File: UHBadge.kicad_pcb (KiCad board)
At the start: 2 copper layers, 0 parts

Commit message: Added footprints.
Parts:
- added C1: 4.7uF, Capacitor_SMD:C_0402_1005Metric, F.Cu at (153.6, 54.0)
- added C10: 100nF, Capacitor_SMD:C_0402_1005Metric, F.Cu at (156.5, 57.9)
- added C11: 100nF, Capacitor_SMD:C_0402_1005Metric, F.Cu at (156.5, 59.9)
- added C12: 100nF, Capacitor_SMD:C_0402_1005Metric, F.Cu at (156.5, 61.9)
- added C13: 100nF, Capacitor_SMD:C_0402_1005Metric, F.Cu at (156.5, 63.8)
- added C14: 100nF, Capacitor_SMD:C_0402_1005Metric, F.Cu at (156.5, 65.8)
- added C15: 100nF, Capacitor_SMD:C_0402_1005Metric, F.Cu at (159.3, 54.0)
- added C16: 4.7uF, Capacitor_SMD:C_0402_1005Metric, F.Cu at (159.3, 56.0)
- added C17: 4.7uF, Capacitor_SMD:C_0402_1005Metric, F.Cu at (159.3, 57.9)
- added C18: 10uF, Capacitor_SMD:C_0402_1005Metric, F.Cu at (159.3, 59.9)
- added C19: 100nF, Capacitor_SMD:C_0402_1005Metric, F.Cu at (159.3, 61.9)
- added C2: 4.7uF, Capacitor_SMD:C_0402_1005Metric, F.Cu at (153.6, 56.0)
- added C20: 15pF, Capacitor_SMD:C_0402_1005Metric, F.Cu at (159.3, 63.8)
- added C21: 15pF, Capacitor_SMD:C_0402_1005Metric, F.Cu at (159.3, 65.8)
- added C22: 33pF, Capacitor_SMD:C_0402_1005Metric, F.Cu at (162.2, 54.0)
- added C23: 0.1uF, Capacitor_SMD:C_0402_1005Metric, F.Cu at (162.2, 56.0)
- added C24: 1uF, Capacitor_SMD:C_0402_1005Metric, F.Cu at (162.2, 57.9)
- added C25: 1uF, Capacitor_SMD:C_0402_1005Metric, F.Cu at (162.2, 59.9)
- added C26: 1uF, Capacitor_SMD:C_0402_1005Metric, F.Cu at (162.2, 61.9)
- added C27: 1uF, Capacitor_SMD:C_0402_1005Metric, F.Cu at (162.2, 63.8)
- added C28: 1uF, Capacitor_SMD:C_0402_1005Metric, F.Cu at (162.2, 65.8)
- added C29: 1uF, Capacitor_SMD:C_0402_1005Metric, F.Cu at (165.1, 54.0)
- added C3: 4.7uF, Capacitor_SMD:C_0402_1005Metric, F.Cu at (153.6, 57.9)
- added C30: 1uF, Capacitor_SMD:C_0402_1005Metric, F.Cu at (165.1, 56.0)
- added C31: 1uF, Capacitor_SMD:C_0402_1005Metric, F.Cu at (165.1, 57.9)
- added C32: 1uF, Capacitor_SMD:C_0402_1005Metric, F.Cu at (165.1, 59.9)
- added C33: 1uF, Capacitor_SMD:C_0402_1005Metric, F.Cu at (165.1, 61.9)
- added C34: 4.7uF, Capacitor_SMD:C_0402_1005Metric, F.Cu at (165.1, 63.8)
- added C35: 4.7uF, Capacitor_SMD:C_0402_1005Metric, F.Cu at (165.1, 65.8)
- added C4: 100nF, Capacitor_SMD:C_0402_1005Metric, F.Cu at (153.6, 59.9)
- added C5: 4.7uF, Capacitor_SMD:C_0402_1005Metric, F.Cu at (153.6, 61.9)
- added C6: 100nF, Capacitor_SMD:C_0402_1005Metric, F.Cu at (153.6, 63.8)
- added C7: 100nF, Capacitor_SMD:C_0402_1005Metric, F.Cu at (153.6, 65.8)
- added C8: 100nF, Capacitor_SMD:C_0402_1005Metric, F.Cu at (156.5, 54.0)
- added C9: 100nF, Capacitor_SMD:C_0402_1005Metric, F.Cu at (156.5, 56.0)
- added D1: LED, LED_SMD:LED_0805_2012Metric, F.Cu at (160.3, 68.3)
- added D2: LED, LED_SMD:LED_0805_2012Metric, F.Cu at (160.3, 71.3)
- added D3: LED, LED_SMD:LED_0805_2012Metric, F.Cu at (160.3, 74.4)
- added D4: LED, LED_SMD:LED_0805_2012Metric, F.Cu at (160.3, 77.4)
- added D5: MBR0530, Diode_SMD:D_SOD-123, F.Cu at (120.9, 93.6)
- added D6: MBR0530, Diode_SMD:D_SOD-123, F.Cu at (120.9, 97.0)
- added D7: MBR0530, Diode_SMD:D_SOD-123, F.Cu at (120.9, 100.3)
- added H1: MountingHole_Pad, MountingHole:MountingHole_2.2mm_M2_Pad_Via, F.Cu at (155.1, 69.8)
- added H2: MountingHole_Pad, MountingHole:MountingHole_2.2mm_M2_Pad_Via, F.Cu at (155.1, 75.7)
- added J1: Conn_01x03_MountingPin, Connector_PinHeader_1.00mm:PinHeader_1x03_P1.00mm_Vertical, F.Cu at (141.9, 99.6)
- added J2: Conn_01x10_MountingPin, Connector_PinHeader_1.00mm:PinHeader_1x10_P1.00mm_Vertical, F.Cu at (164.2, 68.3)
- added L1: 3.3u, CustomFootprints:Inductor, F.Cu at (163.2, 102.9)
- added L2: NFC Antenna, CustomFootprints:NFC_Antenna, F.Cu at (127.2, 91.2)
- added L3: 47uH 500mA, Inductor_SMD:L_APV_ANR4018, F.Cu at (158.3, 100.1)
- added P1: USB_C_Plug_USB2.0, Connector_USB:USB_C_Receptacle_GCT_USB4105-xx-A_16P_TopMnt_Horizontal, F.Cu at (140.9, 93.3)
- added Q1: Si1308EDL, Package_TO_SOT_SMD:SOT-323_SC-70, F.Cu at (132.4, 93.7)
- added R1: 33Ω, Resistor_SMD:R_0402_1005Metric, F.Cu at (148.2, 89.0)
- added R10: 1kΩ, Resistor_SMD:R_0402_1005Metric, F.Cu at (151.2, 95.0)
- added R11: 1kΩ, Resistor_SMD:R_0402_1005Metric, F.Cu at (151.2, 97.0)
- added R12: 10kΩ, Resistor_SMD:R_0402_1005Metric, F.Cu at (151.2, 99.0)
- added R13: 10kΩ, Resistor_SMD:R_0402_1005Metric, F.Cu at (154.1, 89.0)
- added R14: 10kΩ, Resistor_SMD:R_0402_1005Metric, F.Cu at (154.1, 91.0)
- added R15: 47Ω, Resistor_SMD:R_0402_1005Metric, F.Cu at (154.1, 93.0)
- added R16: 1MΩ, Resistor_SMD:R_0402_1005Metric, F.Cu at (154.1, 95.0)
- added R17: 2.2Ω, Resistor_SMD:R_0402_1005Metric, F.Cu at (154.1, 97.0)
- added R2: 27Ω, Resistor_SMD:R_0402_1005Metric, F.Cu at (148.2, 91.0)
- added R3: 27Ω, Resistor_SMD:R_0402_1005Metric, F.Cu at (148.2, 93.0)
- added R4: 5.1kΩ, Resistor_SMD:R_0402_1005Metric, F.Cu at (148.2, 95.0)
- added R5: 470Ω, Resistor_SMD:R_0402_1005Metric, F.Cu at (148.2, 97.0)
- added R6: 470Ω, Resistor_SMD:R_0402_1005Metric, F.Cu at (148.2, 99.0)
- added R7: 470Ω, Resistor_SMD:R_0402_1005Metric, F.Cu at (151.2, 89.0)
- added R8: 0Ω, Resistor_SMD:R_0402_1005Metric, F.Cu at (151.2, 91.0)
- added R9: 1kΩ, Resistor_SMD:R_0402_1005Metric, F.Cu at (151.2, 93.0)
- added SW1: Boot, Button_Switch_THT:SW_PUSH-12mm_Wuerth-430476085716, F.Cu at (137.4, 57.3)
- added SW2: Run, Button_Switch_THT:SW_PUSH-12mm_Wuerth-430476085716, F.Cu at (137.4, 70.8)
- added U1: RP2350A, Package_DFN_QFN:QFN-60-1EP_7x7mm_P0.4mm_EP3.4x3.4mm, F.Cu at (160.5, 92.7)
- added U2: MCP73871, Package_DFN_QFN:QFN-20-1EP_4x4mm_P0.5mm_EP2.5x2.5mm, F.Cu at (127.3, 95.1)
- added U3: W25Q128JVS, Package_SO:SOIC-8_5.3x5.3mm_P1.27mm, F.Cu at (159.9, 83.6)
- added U4: SRV05-4, Package_TO_SOT_SMD:SOT-23-6, F.Cu at (137.7, 100.4)
- added U5: Conn, Connector_FFC-FPC:Jushuo_AFC07-S24FCA-00_1x24-1MP_P0.50_Horizontal, F.Cu at (144.9, 83.4)
- added U6: ST25DV64K-JFR6D3, Package_DFN_QFN:ST_UFDFPN-12-1EP_3x3mm_P0.5mm_EP1.4x2.55mm, F.Cu at (126.8, 100.5)
- added Y1: ABM8-272-T3, Crystal:Crystal_SMD_3225-4Pin_3.2x2.5mm, F.Cu at (132.1, 100.5)

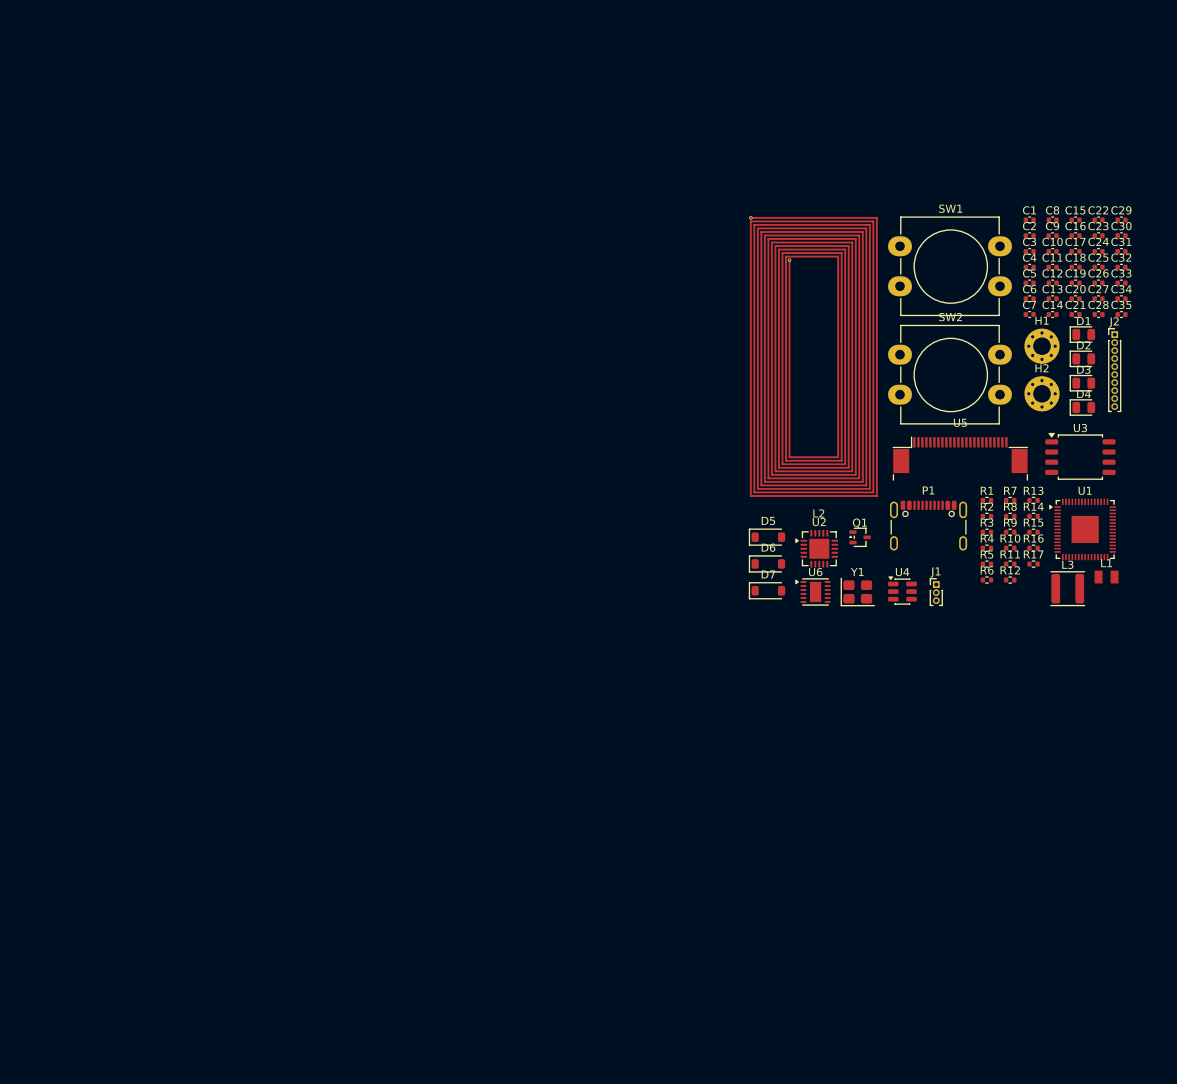
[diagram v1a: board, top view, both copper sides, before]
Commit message: Created the Badge borders. Fixed the buttons footprints.
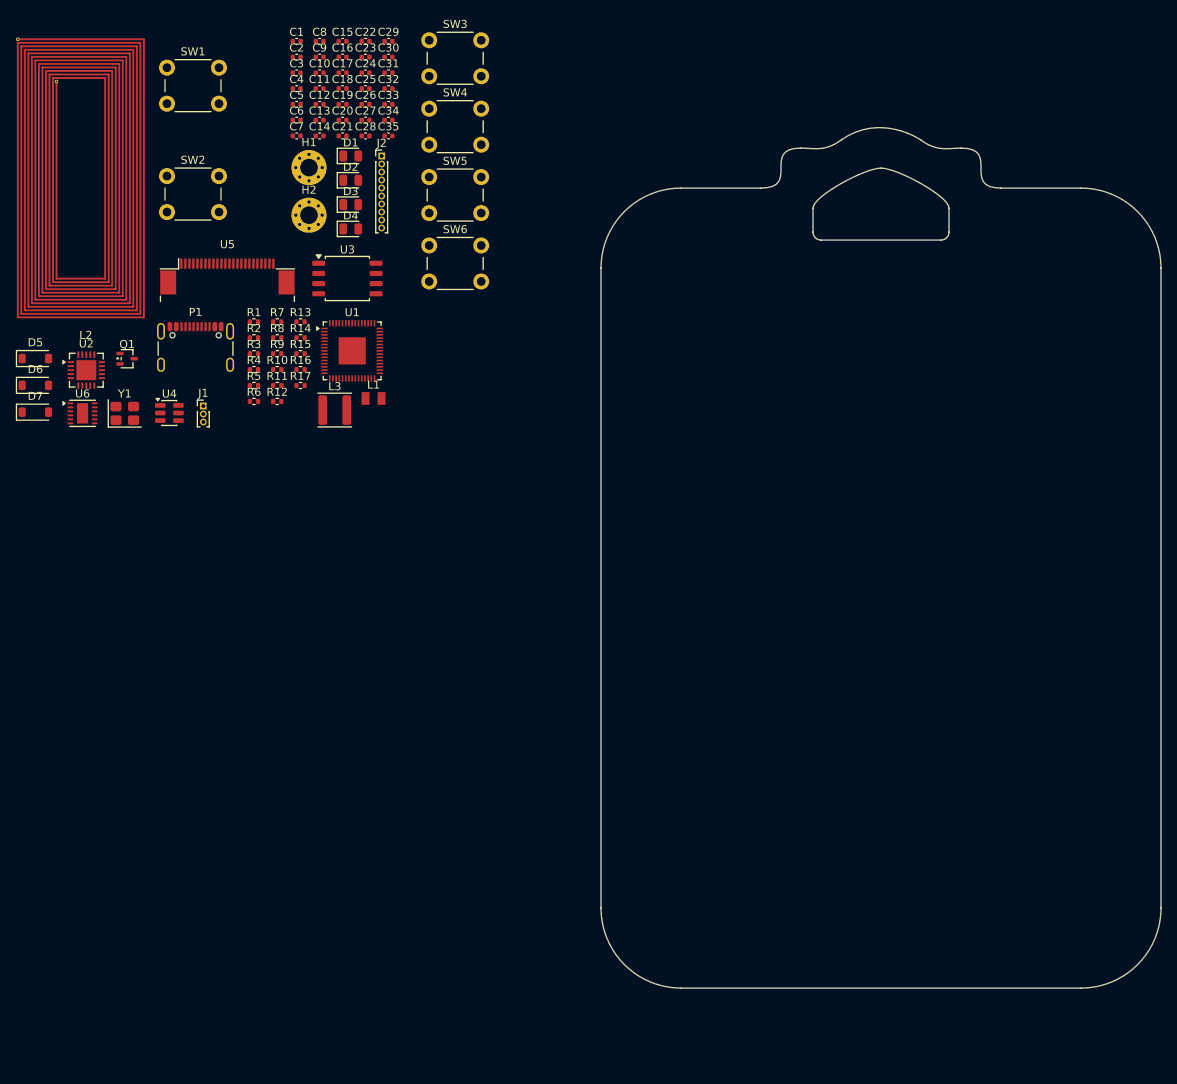
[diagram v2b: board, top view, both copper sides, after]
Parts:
- added SW3: Up, Button_Switch_THT:SW_PUSH_6mm, F.Cu at (78.5, 31.5)
- added SW4: Down, Button_Switch_THT:SW_PUSH_6mm, F.Cu at (78.5, 40.1)
- added SW5: Left, Button_Switch_THT:SW_PUSH_6mm, F.Cu at (78.5, 48.6)
- added SW6: Right, Button_Switch_THT:SW_PUSH_6mm, F.Cu at (78.5, 57.2)
- SW1, SW2: footprint Button_Switch_THT:SW_PUSH-12mm_Wuerth-430476085716 -> Button_Switch_THT:SW_PUSH_6mm
- moved C10 94.3 mm to (64.8, 35.6)
- moved C11 94.3 mm to (64.8, 37.6)
- moved C12 94.3 mm to (64.8, 39.5)
- moved C13 94.3 mm to (64.8, 41.5)
- moved C14 94.3 mm to (64.8, 43.5)
- moved C8 94.3 mm to (64.8, 31.7)
- moved C9 94.3 mm to (64.8, 33.6)
- moved U1 94.3 mm to (68.9, 70.3)
- moved U3 94.3 mm to (68.3, 61.3)
- moved U4 94.3 mm to (46.0, 78.1)
- moved U5 94.3 mm to (53.3, 61.0)
- moved C1 94.3 mm to (62.0, 31.7)
- moved C2 94.3 mm to (62.0, 33.6)
- moved C22 94.3 mm to (70.6, 31.7)
- moved C23 94.3 mm to (70.6, 33.6)
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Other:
- board outline added: 70 x 107.6 mm

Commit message: Connected the buttons to the RP2350.
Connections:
- U1 pad 10: unconnected-(U1-GPIO7-Pad10) -> DOWN
- U1 pad 12: unconnected-(U1-GPIO8-Pad12) -> LEFT
- U1 pad 13: unconnected-(U1-GPIO9-Pad13) -> RIGHT
- U1 pad 9: unconnected-(U1-GPIO6-Pad9) -> UP
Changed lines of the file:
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@@
 			(layers "F.Cu" "F.Mask" "F.Paste")
 			(roundrect_rratio 0.25)
-			(net "unconnected-(U1-GPIO6-Pad9)")
+			(net "UP")
 			(pinfunction "GPIO6_9")
 			(pintype "bidirectional")
@@
 			(layers "F.Cu" "F.Mask" "F.Paste")
 			(roundrect_rratio 0.25)
-			(net "unconnected-(U1-GPIO7-Pad10)")
+			(net "DOWN")
 			(pinfunction "GPIO7_10")
 			(pintype "bidirectional")
@@
 			(layers "F.Cu" "F.Mask" "F.Paste")
 			(roundrect_rratio 0.25)
-			(net "unconnected-(U1-GPIO8-Pad12)")
+			(net "LEFT")
 			(pinfunction "GPIO8_12")
 			(pintype "bidirectional")
@@
 			(layers "F.Cu" "F.Mask" "F.Paste")
 			(roundrect_rratio 0.25)
-			(net "unconnected-(U1-GPIO9-Pad13)")
+			(net "RIGHT")
 			(pinfunction "GPIO9_13")
 			(pintype "bidirectional")

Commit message: Added the e-ink display. Made the button design.
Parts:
- L2, U5: moved to B.Cu
- SW1, SW2, SW3, SW4, SW5, SW6: footprint Button_Switch_THT:SW_PUSH_6mm -> Button_Switch_SMD:SW_SPST_EVQP2_MiddlePushTravel_H2.5mm
- moved L2 126.7 mm to (152.7, 117.3)
- moved SW5 108.8 mm to (120.1, 149.2)
- moved SW4 107.8 mm to (112.5, 142.4), turned to 90 degrees
- moved SW6 106.7 mm to (132.6, 149.2)
- moved SW3 104.2 mm to (112.5, 130.0), turned to 90 degrees
- moved U5 82.0 mm to (135.0, 68.0)
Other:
- board size 70 x 107.6 mm -> 70 x 117.6 mm

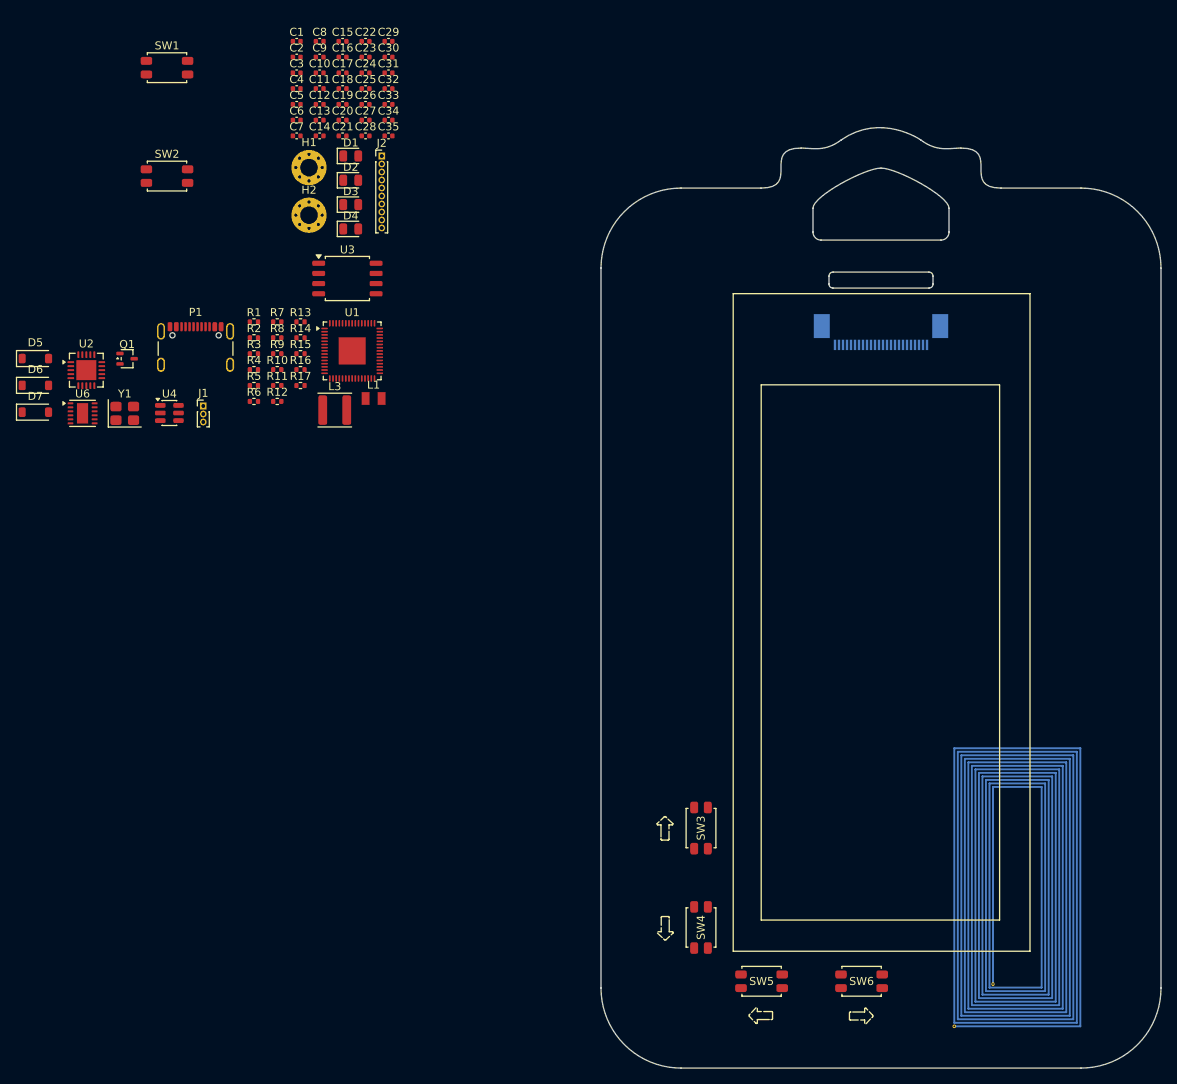
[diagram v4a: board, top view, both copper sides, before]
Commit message: Connected the support components to the e-ink display. Placed the RP2350 and started connecting the support components.
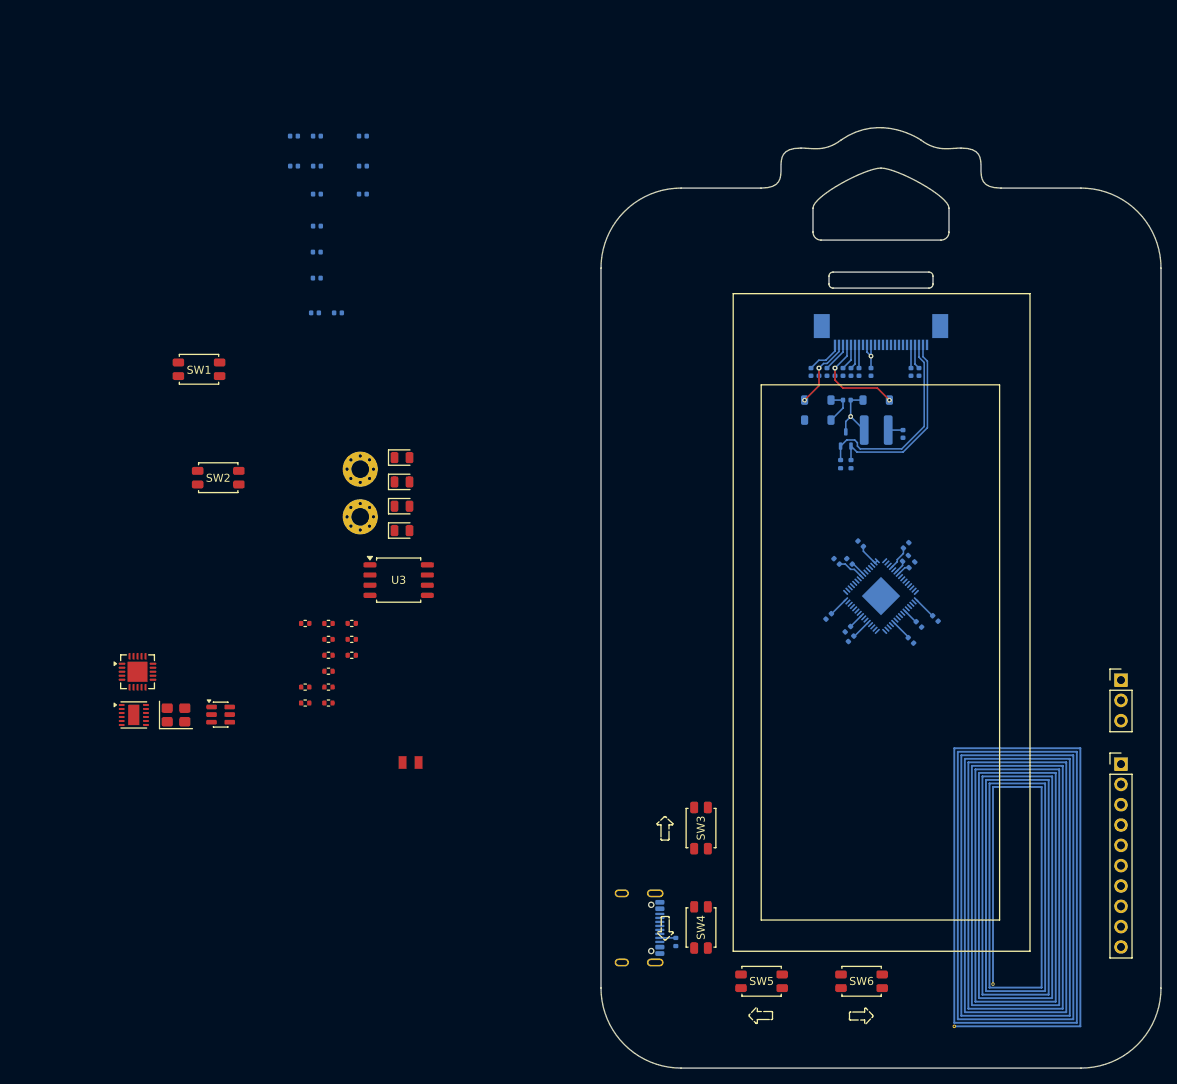
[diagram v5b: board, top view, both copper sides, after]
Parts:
- C1, C10, C11, C12, C13, C14, C15, C16, C17, C18, C19, C2, C20, C21, C22, C23, C24, C25, C26, C27, C28, C29, C3, C30, C31, C32, C33, C34, C35, C4, C6, C7, C8, C9, D5, D6, D7, L3, P1, Q1, R16, R17, R2, R3, R4, U1: moved to B.Cu
- C5: value 4.7uF -> 100nF; moved to B.Cu
- J1: footprint Connector_PinHeader_1.00mm:PinHeader_1x03_P1.00mm_Vertical -> Connector_PinHeader_2.54mm:PinHeader_1x03_P2.54mm_Vertical
- J2: footprint Connector_PinHeader_1.00mm:PinHeader_1x10_P1.00mm_Vertical -> Connector_PinHeader_2.54mm:PinHeader_1x10_P2.54mm_Vertical
- moved J1 119.7 mm to (165.0, 111.5)
- moved J2 119.7 mm to (165.0, 122.0)
- moved D7 105.1 mm to (134.4, 76.5), turned to 180 degrees
- moved C6 100.1 mm to (139.7, 104.5), turned to -45 degrees
- moved C7 100.1 mm to (141.8, 103.8), turned to -45 degrees
- moved C13 98.4 mm to (138.7, 106.5), turned to -45 degrees
- moved D5 98.1 mm to (127.1, 79.0)
- moved D6 97.8 mm to (127.1, 76.5), turned to 180 degrees
- moved C8 96.7 mm to (138.1, 94.7), turned to 45 degrees
- moved C5 95.1 mm to (130.9, 105.1), turned to -135 degrees
- moved C12 94.2 mm to (131.3, 106.3), turned to -135 degrees
- moved C11 91.7 mm to (128.5, 103.5), turned to -135 degrees
- moved C9 91.0 mm to (132.5, 94.5), turned to 135 degrees
- moved C4 90.9 mm to (131.1, 96.7), turned to 135 degrees
- moved Q1 90.4 mm to (130.6, 81.4), turned to 90 degrees
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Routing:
- net RP2350_DECOUPLING_IOVDD+: track 0.00 -> 26.4 mm, vias 0 -> 1
- net E-INK_RESE: track 0.00 -> 24.9 mm
- net E-INK_GDR: track 0.00 -> 23.5 mm
- net E-INK_VGH: track 0.00 -> 12.9 mm, vias 0 -> 2
- net E-INK_VGL: track 0.00 -> 8.94 mm, vias 0 -> 2
- net Net-(D7-A): track 0.00 -> 8.16 mm, vias 0 -> 1
- net RP2350_DECOUPLING_DVDD: track 0.00 -> 5.84 mm
- net Net-(U5-VCOM): track 0.00 -> 4.65 mm
- net Net-(D5-A): track 0.00 -> 4.62 mm
- net Net-(U5-VSL): track 0.00 -> 3.73 mm
- net Net-(U5-VSH1): track 0.00 -> 3.31 mm
- net Net-(U5-VPP): track 0.00 -> 3.11 mm
- net Net-(U5-VGL/NC): track 0.00 -> 3.11 mm
- net Net-(U5-VSH2): track 0.00 -> 2.90 mm
- net Net-(U5-VDD): track 0.00 -> 2.90 mm
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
